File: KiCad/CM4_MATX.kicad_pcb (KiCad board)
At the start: 2 copper layers, 243.8 x 243.8 mm, 74 parts, among them IC1 USB2517-JZX, IC2 PI7C9X2G404SLBFDE, IC3 M24C04-RMN6TP, J1 CM4_B, J10 72309-8014BLF, J11 10104110-0001LF, J12 SS-52100-002, J13 PCIe_x16, J14 PCIe_x16, J15 PCIe_x16, J16 GSD090012SEU, J17 Conn_02x04_Odd_Even, J18 ARJM11C7-502-AB-ER2-T, J19 Conn_02x20_Odd_Even, J2 CM4_A, J20 Conn_02x04_Odd_Even, J3 Conn_01x22_Female, J4 72309-8014BLF, J5 Conn_01x22_Female, J6 1888811-1, J7 39-28-1243, J9 Conn_02x05_Odd_Even, M1 Fan_CPU_4pin, M2 Fan_CPU_4pin, U1 MAX6639ATE+, U10 MIC2019YM6-TR, U11 MIC2019YM6-TR, U12 MIC2019YM6-TR, U13 MIC2019YM6-TR, U14 MIC2019YM6-TR, U15 MIC2019YM6-TR, U16 MIC2019YM6-TR, U17 TCA9548ARGER, U18 PCF85263AT, U19 AP7363-10D, U3 FSUSB42MUX, U4 AP7363-10D, U5 AP2822CKETR-G1, U6 74LVC1G07GW, U7 TPD4EUSB30, U8 RT9742GGJ5, U9 TPD4EUSB30, Y2 32.768KHz

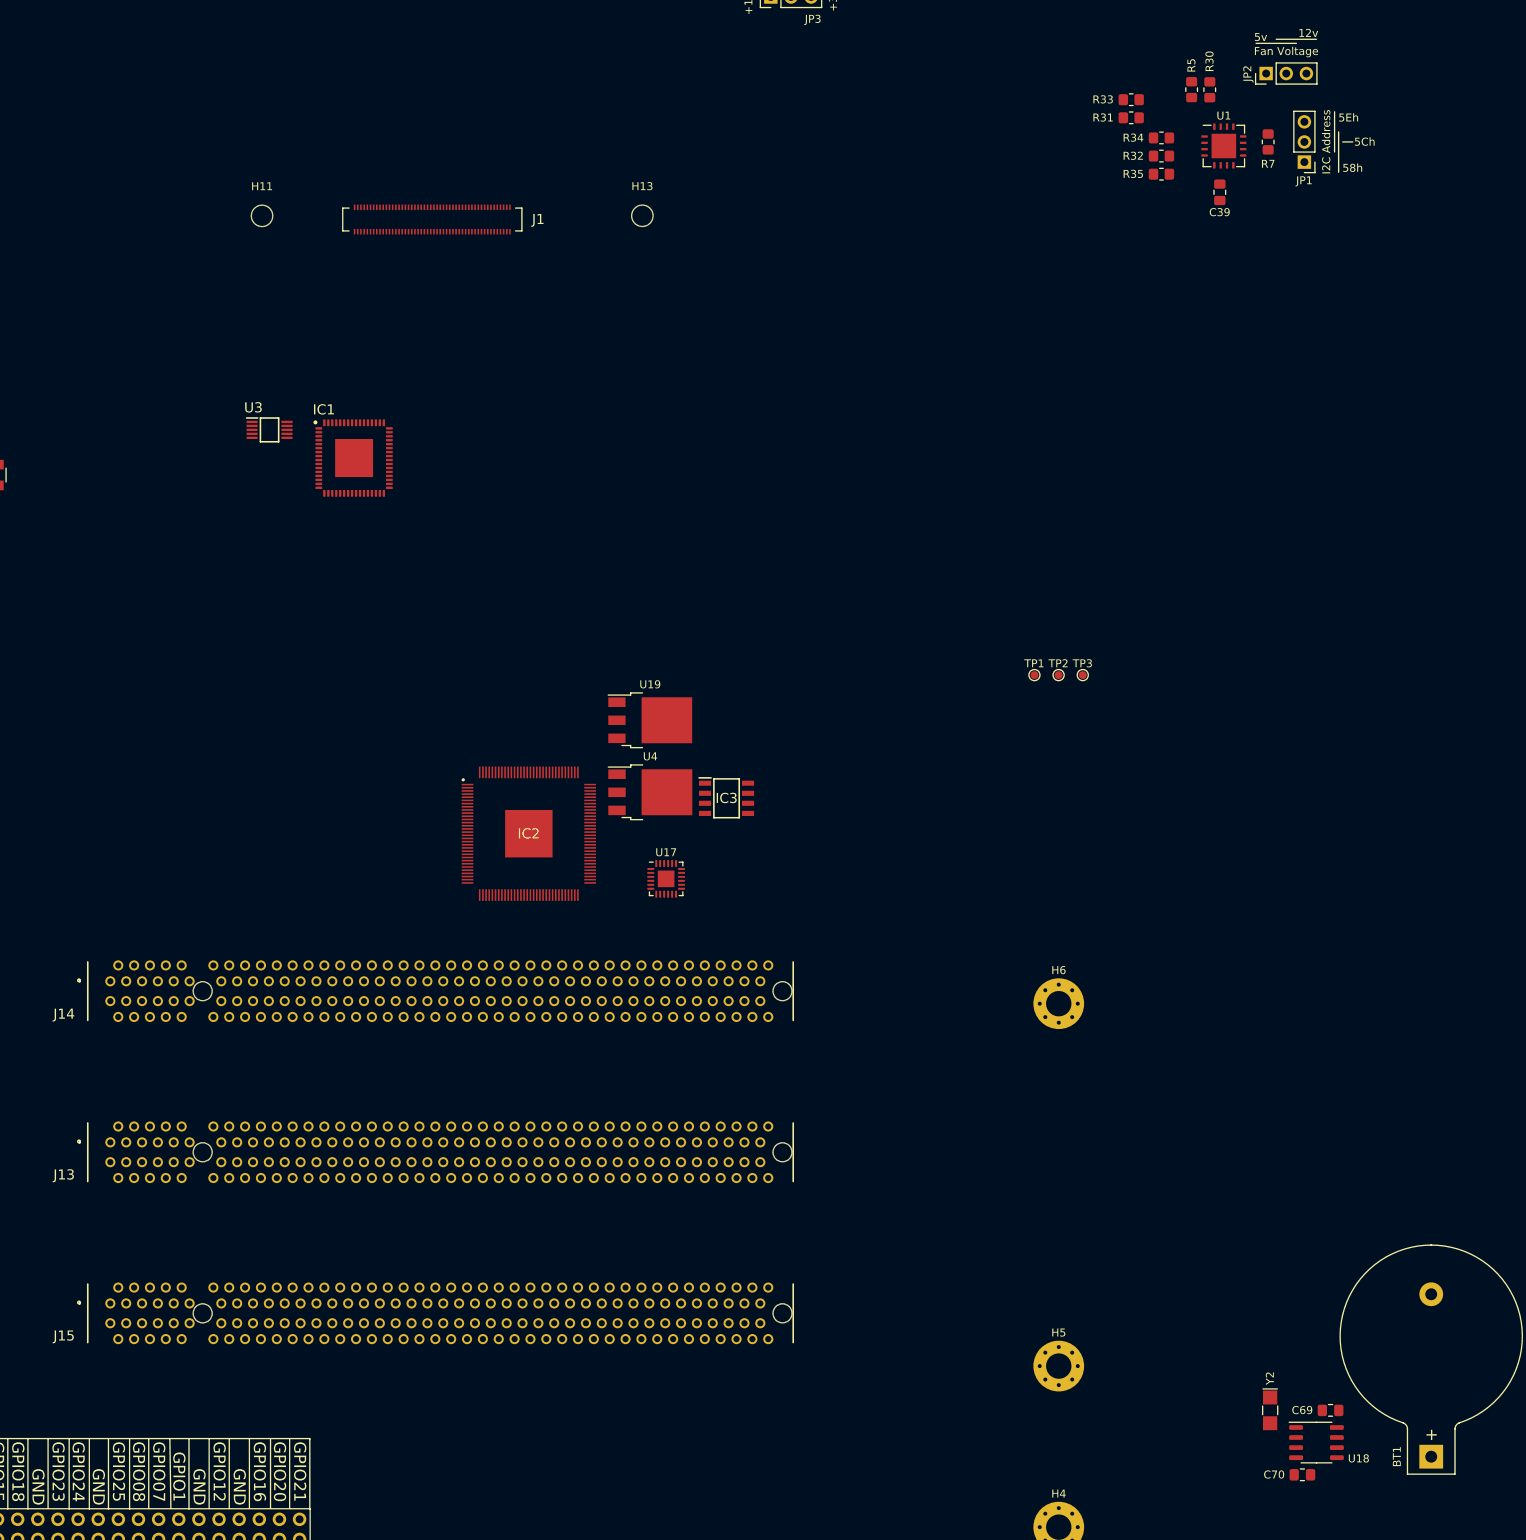
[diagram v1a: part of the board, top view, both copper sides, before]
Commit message: Imported new components to the PCB and moved some components
Updated PDFs and added two new board layers. One for ground and a second for power (voltage to be decided)
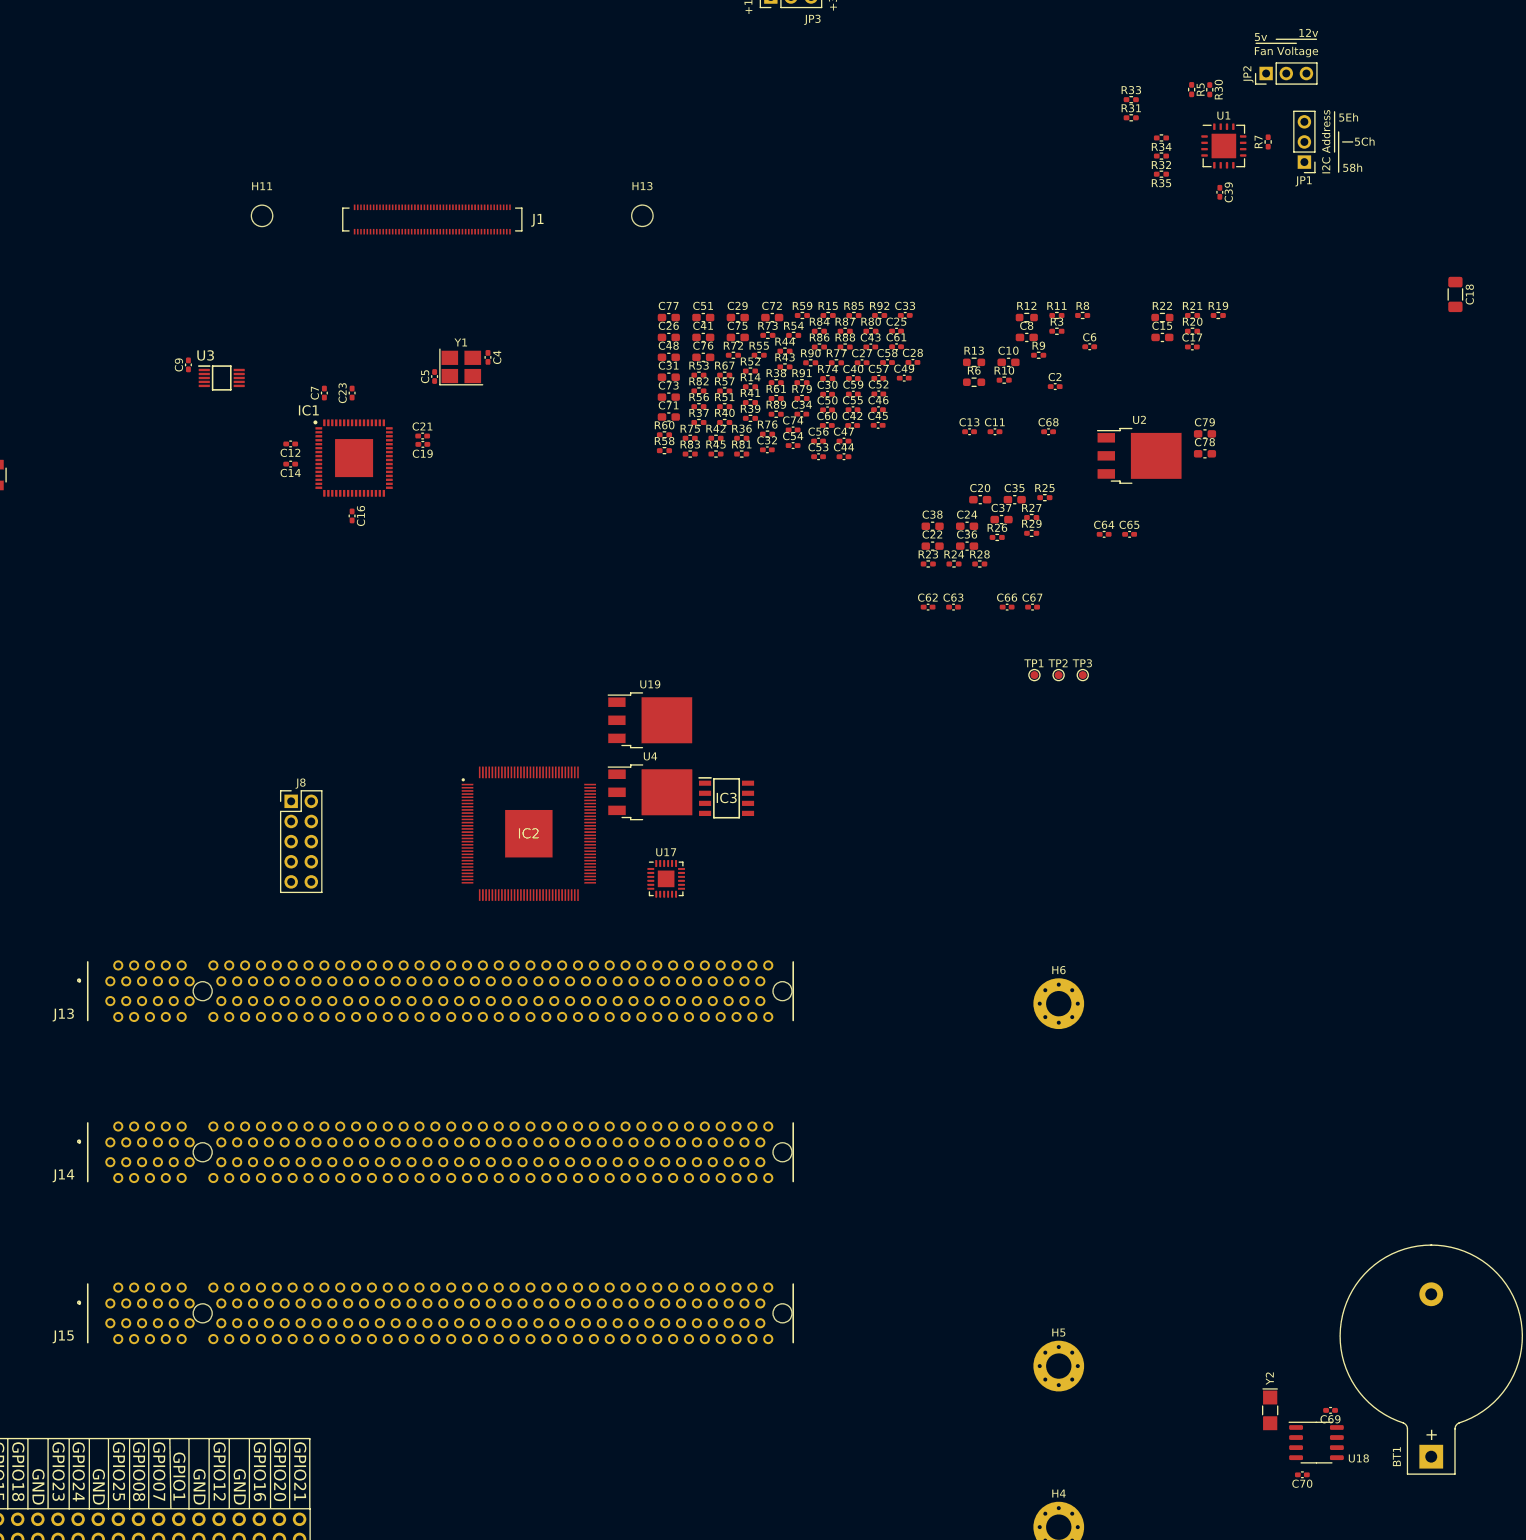
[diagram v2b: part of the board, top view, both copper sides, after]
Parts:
- added C10: 10uF, CM4_MATX:C_0603_1608Metric_Pad1.08x0.95mm_HandSolder, F.Cu at (196.9, 105.8)
- added C11: 100nF, CM4_MATX:C_0402_1005Metric_Pad0.74x0.62mm_HandSolder, F.Cu at (195.2, 114.5)
- added C12: 100nF, CM4_MATX:C_0402_1005Metric_Pad0.74x0.62mm_HandSolder, F.Cu at (106.3, 116.1)
- added C13: 100nF, CM4_MATX:C_0402_1005Metric_Pad0.74x0.62mm_HandSolder, F.Cu at (191.9, 114.5)
- added C14: 100nF, CM4_MATX:C_0402_1005Metric_Pad0.74x0.62mm_HandSolder, F.Cu at (106.3, 118.6)
- added C15: 10uF, CM4_MATX:C_0603_1608Metric_Pad1.08x0.95mm_HandSolder, F.Cu at (216.3, 102.6)
- added C16: 100nF, CM4_MATX:C_0402_1005Metric_Pad0.74x0.62mm_HandSolder, F.Cu at (114.0, 125.2)
- added C17: 100nF, CM4_MATX:C_0402_1005Metric_Pad0.74x0.62mm_HandSolder, F.Cu at (220.1, 103.8)
- added C18: 100uF, CM4_MATX:C_1206_3216Metric_Pad1.33x1.80mm_HandSolder, F.Cu at (253.2, 97.2)
- added C19: 100nF, CM4_MATX:C_0402_1005Metric_Pad0.74x0.62mm_HandSolder, F.Cu at (123.0, 116.1)
- added C2: 100nF, CM4_MATX:C_0402_1005Metric_Pad0.74x0.62mm_HandSolder, F.Cu at (202.8, 108.8)
- added C20: 10uF, CM4_MATX:C_0603_1608Metric_Pad1.08x0.95mm_HandSolder, F.Cu at (193.3, 123.1)
- added C21: 100nF, CM4_MATX:C_0402_1005Metric_Pad0.74x0.62mm_HandSolder, F.Cu at (122.9, 115.1)
- added C22: 10uF, CM4_MATX:C_0603_1608Metric_Pad1.08x0.95mm_HandSolder, F.Cu at (187.3, 129.0)
- added C23: 100nF, CM4_MATX:C_0402_1005Metric_Pad0.74x0.62mm_HandSolder, F.Cu at (114.0, 109.7)
- added C24: 10uF, CM4_MATX:C_0603_1608Metric_Pad1.08x0.95mm_HandSolder, F.Cu at (191.6, 126.5)
- added C25: 100nF, CM4_MATX:C_0402_1005Metric_Pad0.74x0.62mm_HandSolder, F.Cu at (182.7, 101.8)
- added C26: 10uF, CM4_MATX:C_0603_1608Metric_Pad1.08x0.95mm_HandSolder, F.Cu at (154.0, 102.6)
- added C27: 100nF, CM4_MATX:C_0402_1005Metric_Pad0.74x0.62mm_HandSolder, F.Cu at (178.4, 105.8)
- added C28: 100nF, CM4_MATX:C_0402_1005Metric_Pad0.74x0.62mm_HandSolder, F.Cu at (184.8, 105.8)
- added C29: 10uF, CM4_MATX:C_0603_1608Metric_Pad1.08x0.95mm_HandSolder, F.Cu at (162.7, 100.1)
- added C30: 100nF, CM4_MATX:C_0402_1005Metric_Pad0.74x0.62mm_HandSolder, F.Cu at (174.0, 109.8)
- added C31: 10uF, CM4_MATX:C_0603_1608Metric_Pad1.08x0.95mm_HandSolder, F.Cu at (154.0, 107.7)
- added C32: 100nF, CM4_MATX:C_0402_1005Metric_Pad0.74x0.62mm_HandSolder, F.Cu at (166.4, 116.8)
- added C33: 100nF, CM4_MATX:C_0402_1005Metric_Pad0.74x0.62mm_HandSolder, F.Cu at (183.8, 99.9)
- added C34: 100nF, CM4_MATX:C_0402_1005Metric_Pad0.74x0.62mm_HandSolder, F.Cu at (170.8, 112.3)
- added C35: 10uF, CM4_MATX:C_0603_1608Metric_Pad1.08x0.95mm_HandSolder, F.Cu at (197.6, 123.1)
- added C36: 10uF, CM4_MATX:C_0603_1608Metric_Pad1.08x0.95mm_HandSolder, F.Cu at (191.6, 129.0)
- added C37: 10uF, CM4_MATX:C_0603_1608Metric_Pad1.08x0.95mm_HandSolder, F.Cu at (196.0, 125.6)
- added C38: 10uF, CM4_MATX:C_0603_1608Metric_Pad1.08x0.95mm_HandSolder, F.Cu at (187.3, 126.5)
- added C4: 16pF, CM4_MATX:C_0402_1005Metric_Pad0.74x0.62mm_HandSolder, F.Cu at (131.2, 105.2)
- added C40: 100nF, CM4_MATX:C_0402_1005Metric_Pad0.74x0.62mm_HandSolder, F.Cu at (177.3, 107.8)
- added C41: 10uF, CM4_MATX:C_0603_1608Metric_Pad1.08x0.95mm_HandSolder, F.Cu at (158.4, 102.6)
- added C42: 100nF, CM4_MATX:C_0402_1005Metric_Pad0.74x0.62mm_HandSolder, F.Cu at (177.2, 113.7)
- added C43: 100nF, CM4_MATX:C_0402_1005Metric_Pad0.74x0.62mm_HandSolder, F.Cu at (179.5, 103.8)
- added C44: 100nF, CM4_MATX:C_0402_1005Metric_Pad0.74x0.62mm_HandSolder, F.Cu at (176.1, 117.7)
- added C45: 100nF, CM4_MATX:C_0402_1005Metric_Pad0.74x0.62mm_HandSolder, F.Cu at (180.4, 113.7)
- added C46: 100nF, CM4_MATX:C_0402_1005Metric_Pad0.74x0.62mm_HandSolder, F.Cu at (180.5, 111.8)
- added C47: 100nF, CM4_MATX:C_0402_1005Metric_Pad0.74x0.62mm_HandSolder, F.Cu at (176.1, 115.7)
- added C48: 10uF, CM4_MATX:C_0603_1608Metric_Pad1.08x0.95mm_HandSolder, F.Cu at (154.0, 105.1)
- added C49: 100nF, CM4_MATX:C_0402_1005Metric_Pad0.74x0.62mm_HandSolder, F.Cu at (183.7, 107.8)
- added C5: 16pF, CM4_MATX:C_0402_1005Metric_Pad0.74x0.62mm_HandSolder, F.Cu at (124.5, 107.6)
- added C50: 100nF, CM4_MATX:C_0402_1005Metric_Pad0.74x0.62mm_HandSolder, F.Cu at (174.0, 111.8)
- added C51: 10uF, CM4_MATX:C_0603_1608Metric_Pad1.08x0.95mm_HandSolder, F.Cu at (158.4, 100.1)
- added C52: 100nF, CM4_MATX:C_0402_1005Metric_Pad0.74x0.62mm_HandSolder, F.Cu at (180.5, 109.8)
- added C53: 100nF, CM4_MATX:C_0402_1005Metric_Pad0.74x0.62mm_HandSolder, F.Cu at (172.9, 117.7)
- added C54: 100nF, CM4_MATX:C_0402_1005Metric_Pad0.74x0.62mm_HandSolder, F.Cu at (169.7, 116.3)
- added C55: 100nF, CM4_MATX:C_0402_1005Metric_Pad0.74x0.62mm_HandSolder, F.Cu at (177.2, 111.8)
- added C56: 100nF, CM4_MATX:C_0402_1005Metric_Pad0.74x0.62mm_HandSolder, F.Cu at (172.9, 115.7)
- added C57: 100nF, CM4_MATX:C_0402_1005Metric_Pad0.74x0.62mm_HandSolder, F.Cu at (180.5, 107.8)
- added C58: 100nF, CM4_MATX:C_0402_1005Metric_Pad0.74x0.62mm_HandSolder, F.Cu at (181.6, 105.8)
- added C59: 100nF, CM4_MATX:C_0402_1005Metric_Pad0.74x0.62mm_HandSolder, F.Cu at (177.3, 109.8)
- added C6: 100nF, CM4_MATX:C_0402_1005Metric_Pad0.74x0.62mm_HandSolder, F.Cu at (207.1, 103.8)
- added C60: 100nF, CM4_MATX:C_0402_1005Metric_Pad0.74x0.62mm_HandSolder, F.Cu at (174.0, 113.7)
- added C61: 100nF, CM4_MATX:C_0402_1005Metric_Pad0.74x0.62mm_HandSolder, F.Cu at (182.7, 103.8)
- added C62: 100nF, CM4_MATX:C_0402_1005Metric_Pad0.74x0.62mm_HandSolder, F.Cu at (186.7, 136.7)
- added C63: 100nF, CM4_MATX:C_0402_1005Metric_Pad0.74x0.62mm_HandSolder, F.Cu at (189.9, 136.7)
- added C64: 100nF, CM4_MATX:C_0402_1005Metric_Pad0.74x0.62mm_HandSolder, F.Cu at (208.9, 127.5)
- added C65: 100nF, CM4_MATX:C_0402_1005Metric_Pad0.74x0.62mm_HandSolder, F.Cu at (212.1, 127.5)
- added C66: 100nF, CM4_MATX:C_0402_1005Metric_Pad0.74x0.62mm_HandSolder, F.Cu at (196.7, 136.7)
- added C67: 100nF, CM4_MATX:C_0402_1005Metric_Pad0.74x0.62mm_HandSolder, F.Cu at (199.9, 136.7)
- added C68: 100nF, CM4_MATX:C_0402_1005Metric_Pad0.74x0.62mm_HandSolder, F.Cu at (201.9, 114.5)
- added C7: 100nF, CM4_MATX:C_0402_1005Metric_Pad0.74x0.62mm_HandSolder, F.Cu at (110.5, 109.7)
- added C71: 10uF, CM4_MATX:C_0603_1608Metric_Pad1.08x0.95mm_HandSolder, F.Cu at (154.0, 112.7)
- added C72: 10uF, CM4_MATX:C_0603_1608Metric_Pad1.08x0.95mm_HandSolder, F.Cu at (167.1, 100.1)
- added C73: 10uF, CM4_MATX:C_0603_1608Metric_Pad1.08x0.95mm_HandSolder, F.Cu at (154.0, 110.2)
- added C74: 100nF, CM4_MATX:C_0402_1005Metric_Pad0.74x0.62mm_HandSolder, F.Cu at (169.7, 114.3)
- added C75: 10uF, CM4_MATX:C_0603_1608Metric_Pad1.08x0.95mm_HandSolder, F.Cu at (162.7, 102.6)
- added C76: 10uF, CM4_MATX:C_0603_1608Metric_Pad1.08x0.95mm_HandSolder, F.Cu at (158.4, 105.1)
- added C77: 10uF, CM4_MATX:C_0603_1608Metric_Pad1.08x0.95mm_HandSolder, F.Cu at (154.0, 100.1)
- added C78: 10uF, CM4_MATX:C_0603_1608Metric_Pad1.08x0.95mm_HandSolder, F.Cu at (221.6, 117.3)
- added C79: 10uF, CM4_MATX:C_0603_1608Metric_Pad1.08x0.95mm_HandSolder, F.Cu at (221.6, 114.8)
- added C8: 10uF, CM4_MATX:C_0603_1608Metric_Pad1.08x0.95mm_HandSolder, F.Cu at (199.2, 102.6)
- added C9: 100nF, CM4_MATX:C_0402_1005Metric_Pad0.74x0.62mm_HandSolder, F.Cu at (93.4, 106.1)
- added J8: Conn_02x05_Odd_Even, CM4_MATX:PinHeader_2x05_P2.54mm_Vertical, F.Cu at (106.4, 161.2)
- added R10: 100K 5%, CM4_MATX:R_0402_1005Metric_Pad0.72x0.64mm_HandSolder, F.Cu at (196.3, 108.0)
- added R11: 100K 5%, CM4_MATX:R_0402_1005Metric_Pad0.72x0.64mm_HandSolder, F.Cu at (203.0, 99.9)
- added R12: 2.2K 1%, CM4_MATX:R_0603_1608Metric_Pad0.98x0.95mm_HandSolder, F.Cu at (199.2, 100.1)
- added R13: 2.2K 1%, CM4_MATX:R_0603_1608Metric_Pad0.98x0.95mm_HandSolder, F.Cu at (192.5, 105.8)
- added R14: 475 1%, CM4_MATX:R_0402_1005Metric_Pad0.72x0.64mm_HandSolder, F.Cu at (164.3, 108.9)
- added R15: 1.43k 1%, CM4_MATX:R_0402_1005Metric_Pad0.72x0.64mm_HandSolder, F.Cu at (174.1, 99.9)
- added R19: 1K 1%, CM4_MATX:R_0402_1005Metric_Pad0.72x0.64mm_HandSolder, F.Cu at (223.3, 99.9)
- added R20: 470 1%, CM4_MATX:R_0402_1005Metric_Pad0.72x0.64mm_HandSolder, F.Cu at (220.1, 101.9)
- added R21: 470 1%, CM4_MATX:R_0402_1005Metric_Pad0.72x0.64mm_HandSolder, F.Cu at (220.1, 99.9)
- added R22: 12K 1%, CM4_MATX:R_0603_1608Metric_Pad0.98x0.95mm_HandSolder, F.Cu at (216.3, 100.1)
- added R23: 143 1%, CM4_MATX:R_0402_1005Metric_Pad0.72x0.64mm_HandSolder, F.Cu at (186.7, 131.2)
- added R24: 143 1%, CM4_MATX:R_0402_1005Metric_Pad0.72x0.64mm_HandSolder, F.Cu at (190.0, 131.2)
- added R25: 143 1%, CM4_MATX:R_0402_1005Metric_Pad0.72x0.64mm_HandSolder, F.Cu at (201.4, 122.8)
- added R26: 143 1%, CM4_MATX:R_0402_1005Metric_Pad0.72x0.64mm_HandSolder, F.Cu at (195.4, 127.9)
- added R27: 143 1%, CM4_MATX:R_0402_1005Metric_Pad0.72x0.64mm_HandSolder, F.Cu at (199.8, 125.4)
- added R28: 143 1%, CM4_MATX:R_0402_1005Metric_Pad0.72x0.64mm_HandSolder, F.Cu at (193.2, 131.2)
- added R29: 143 1%, CM4_MATX:R_0402_1005Metric_Pad0.72x0.64mm_HandSolder, F.Cu at (199.8, 127.3)
- added R3: 100K 5%, CM4_MATX:R_0402_1005Metric_Pad0.72x0.64mm_HandSolder, F.Cu at (203.0, 101.9)
- added R36: 330, CM4_MATX:R_0402_1005Metric_Pad0.72x0.64mm_HandSolder, F.Cu at (163.2, 115.4)
- added R37: 330, CM4_MATX:R_0402_1005Metric_Pad0.72x0.64mm_HandSolder, F.Cu at (157.8, 113.4)
- added R38: 330, CM4_MATX:R_0402_1005Metric_Pad0.72x0.64mm_HandSolder, F.Cu at (167.6, 108.3)
- added R39: 330, CM4_MATX:R_0402_1005Metric_Pad0.72x0.64mm_HandSolder, F.Cu at (164.3, 112.8)
- added R40: 330, CM4_MATX:R_0402_1005Metric_Pad0.72x0.64mm_HandSolder, F.Cu at (161.1, 113.4)
- added R41: 5.1k, CM4_MATX:R_0402_1005Metric_Pad0.72x0.64mm_HandSolder, F.Cu at (164.3, 110.9)
- added R42: 5.1k, CM4_MATX:R_0402_1005Metric_Pad0.72x0.64mm_HandSolder, F.Cu at (160.0, 115.4)
- added R43: 5.1k, CM4_MATX:R_0402_1005Metric_Pad0.72x0.64mm_HandSolder, F.Cu at (168.7, 106.4)
- added R44: 5.1k, CM4_MATX:R_0402_1005Metric_Pad0.72x0.64mm_HandSolder, F.Cu at (168.7, 104.4)
- added R45: 5.1k, CM4_MATX:R_0402_1005Metric_Pad0.72x0.64mm_HandSolder, F.Cu at (160.0, 117.3)
- added R51: 5.1k, CM4_MATX:R_0402_1005Metric_Pad0.72x0.64mm_HandSolder, F.Cu at (161.1, 111.4)
- added R52: 5.1k, CM4_MATX:R_0402_1005Metric_Pad0.72x0.64mm_HandSolder, F.Cu at (164.3, 106.9)
- added R53: 5.1k, CM4_MATX:R_0402_1005Metric_Pad0.72x0.64mm_HandSolder, F.Cu at (157.8, 107.4)
- added R54: 33, CM4_MATX:R_0402_1005Metric_Pad0.72x0.64mm_HandSolder, F.Cu at (169.8, 102.4)
- added R55: 33, CM4_MATX:R_0402_1005Metric_Pad0.72x0.64mm_HandSolder, F.Cu at (165.4, 104.9)
- added R56: 33, CM4_MATX:R_0402_1005Metric_Pad0.72x0.64mm_HandSolder, F.Cu at (157.8, 111.4)
- added R57: 33, CM4_MATX:R_0402_1005Metric_Pad0.72x0.64mm_HandSolder, F.Cu at (161.1, 109.4)
- added R58: 33, CM4_MATX:R_0402_1005Metric_Pad0.72x0.64mm_HandSolder, F.Cu at (153.5, 116.9)
- added R59: 33, CM4_MATX:R_0402_1005Metric_Pad0.72x0.64mm_HandSolder, F.Cu at (170.9, 99.9)
- added R6: 12K 1%, CM4_MATX:R_0603_1608Metric_Pad0.98x0.95mm_HandSolder, F.Cu at (192.5, 108.3)
- added R60: 33, CM4_MATX:R_0402_1005Metric_Pad0.72x0.64mm_HandSolder, F.Cu at (153.5, 114.9)
- added R61: 33, CM4_MATX:R_0402_1005Metric_Pad0.72x0.64mm_HandSolder, F.Cu at (167.6, 110.3)
- added R67: 5.1k, CM4_MATX:R_0402_1005Metric_Pad0.72x0.64mm_HandSolder, F.Cu at (161.1, 107.4)
- added R72: 5.1k, CM4_MATX:R_0402_1005Metric_Pad0.72x0.64mm_HandSolder, F.Cu at (162.2, 104.9)
- added R73: 330, CM4_MATX:R_0402_1005Metric_Pad0.72x0.64mm_HandSolder, F.Cu at (166.5, 102.4)
- added R74: 330, CM4_MATX:R_0402_1005Metric_Pad0.72x0.64mm_HandSolder, F.Cu at (174.1, 107.8)
- added R75: 330, CM4_MATX:R_0402_1005Metric_Pad0.72x0.64mm_HandSolder, F.Cu at (156.7, 115.4)
- added R76: 330, CM4_MATX:R_0402_1005Metric_Pad0.72x0.64mm_HandSolder, F.Cu at (166.5, 114.8)
- added R77: 330, CM4_MATX:R_0402_1005Metric_Pad0.72x0.64mm_HandSolder, F.Cu at (175.2, 105.8)
- added R79: 330, CM4_MATX:R_0402_1005Metric_Pad0.72x0.64mm_HandSolder, F.Cu at (170.8, 110.3)
- added R8: 100K 5%, CM4_MATX:R_0402_1005Metric_Pad0.72x0.64mm_HandSolder, F.Cu at (206.2, 99.9)
- added R80: 330, CM4_MATX:R_0402_1005Metric_Pad0.72x0.64mm_HandSolder, F.Cu at (179.5, 101.9)
- added R81: 330, CM4_MATX:R_0402_1005Metric_Pad0.72x0.64mm_HandSolder, F.Cu at (163.2, 117.3)
- added R82: 330, CM4_MATX:R_0402_1005Metric_Pad0.72x0.64mm_HandSolder, F.Cu at (157.8, 109.4)
- added R83: 49.9, CM4_MATX:R_0402_1005Metric_Pad0.72x0.64mm_HandSolder, F.Cu at (156.7, 117.3)
- added R84: 49.9, CM4_MATX:R_0402_1005Metric_Pad0.72x0.64mm_HandSolder, F.Cu at (173.0, 101.9)
- added R85: 49.9, CM4_MATX:R_0402_1005Metric_Pad0.72x0.64mm_HandSolder, F.Cu at (177.4, 99.9)
- added R86: 49.9, CM4_MATX:R_0402_1005Metric_Pad0.72x0.64mm_HandSolder, F.Cu at (173.0, 103.8)
- added R87: 49.9, CM4_MATX:R_0402_1005Metric_Pad0.72x0.64mm_HandSolder, F.Cu at (176.3, 101.9)
- added R88: 49.9, CM4_MATX:R_0402_1005Metric_Pad0.72x0.64mm_HandSolder, F.Cu at (176.3, 103.8)
- added R89: 49.9, CM4_MATX:R_0402_1005Metric_Pad0.72x0.64mm_HandSolder, F.Cu at (167.6, 112.3)
- added R9: 100K 5%, CM4_MATX:R_0402_1005Metric_Pad0.72x0.64mm_HandSolder, F.Cu at (200.7, 104.9)
- added R90: 49.9, CM4_MATX:R_0402_1005Metric_Pad0.72x0.64mm_HandSolder, F.Cu at (171.9, 105.8)
- added R91: 5.1k, CM4_MATX:R_0402_1005Metric_Pad0.72x0.64mm_HandSolder, F.Cu at (170.8, 108.3)
- added R92: 5.1k, CM4_MATX:R_0402_1005Metric_Pad0.72x0.64mm_HandSolder, F.Cu at (180.6, 99.9)
- added U2: AP7363-33D, CM4_MATX:TO-252-3_TabPin2, F.Cu at (213.4, 117.6)
- added Y1: 24MHz, CM4_MATX:Crystal_SMD_3225-4Pin_3.2x2.5mm_HandSoldering, F.Cu at (127.8, 106.4)
- C39: value 0.1uF -> 100nF; footprint CM4_MATX:C_0805_2012Metric_Pad1.18x1.45mm_HandSolder -> CM4_MATX:C_0402_1005Metric_Pad0.74x0.62mm_HandSolder
- C69, C70: footprint CM4_MATX:C_0805_2012Metric_Pad1.18x1.45mm_HandSolder -> CM4_MATX:C_0402_1005Metric_Pad0.74x0.62mm_HandSolder
- H1, H2, H3, H4, H5, H6, H7, H8, H9: footprint MountingHole:MountingHole_3.2mm_M3_Pad_Via -> CM4_MATX:MountingHole_3.2mm_M3_Pad_Via
- H10, H11, H12, H13: footprint MountingHole:MountingHole_2.7mm_M2.5 -> CM4_MATX:MountingHole_2.7mm_M2.5
- IC3: footprint _LibLoader:SOIC127P600X175-8N -> CM4_MATX:SOIC127P600X175-8N
- R30, R31, R32, R33, R34, R35, R5, R7: footprint CM4_MATX:R_0805_2012Metric_Pad1.20x1.40mm_HandSolder -> CM4_MATX:R_0402_1005Metric_Pad0.72x0.64mm_HandSolder
- U17: footprint Package_DFN_QFN:Texas_RGE0024C_EP2.1x2.1mm -> CM4_MATX:Texas_RGE0024C_EP2.1x2.1mm
- moved U3 8.90 mm to (97.6, 107.8)
- renumbered J14 to J13, J13 to J14
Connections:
- net /PCIe_Subsystem/PCIE1_JTAG_TCK renamed Net-(J13-PadA5)
- net /PCIe_Subsystem/PCIE1_JTAG_TDI renamed Net-(J13-PadA6)
- net /PCIe_Subsystem/PCIE1_JTAG_TDO renamed Net-(J13-PadA7)
- net /PCIe_Subsystem/PCIE1_JTAG_TMS renamed Net-(J13-PadA8)
- net /PCIe_Subsystem/PCIE1_JTAG_TRST# renamed Net-(J13-PadB9)
- net /PCIe_Subsystem/PCIE2_JTAG_TCK renamed Net-(J14-PadA5)
- net /PCIe_Subsystem/PCIE2_JTAG_TDI renamed Net-(J14-PadA6)
- net /PCIe_Subsystem/PCIE2_JTAG_TDO renamed Net-(J14-PadA7)
- net /PCIe_Subsystem/PCIE2_JTAG_TMS renamed Net-(J14-PadA8)
- net /PCIe_Subsystem/PCIE2_JTAG_TRST# renamed Net-(J14-PadB9)
- net /PCIe_Subsystem/PCIE3_JTAG_TCK renamed Net-(J15-PadA5)
- net /PCIe_Subsystem/PCIE3_JTAG_TDI renamed Net-(J15-PadA6)
- net /PCIe_Subsystem/PCIE3_JTAG_TDO renamed Net-(J15-PadA7)
- net /PCIe_Subsystem/PCIE3_JTAG_TMS renamed Net-(J15-PadA8)
- net /PCIe_Subsystem/PCIE3_JTAG_TRST# renamed Net-(J15-PadB9)
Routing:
- added copper zone on In1.Cu, net GND
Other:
- copper layers 2 -> 4

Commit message: Added some DRC specifics
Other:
- rule trace_min: 0.2 -> 0.0889
- rule via_min_drill: 0.3 -> 0.2
- rule via_min_size: 0.4 -> 0.45

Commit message: Added Planes
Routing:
- added copper zone on In2.Cu, net +3V3
- added copper zone on In2.Cu, net /+5v
